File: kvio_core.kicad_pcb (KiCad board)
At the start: 6 copper layers, 60 x 41 mm, 214 parts, among them J1001 16-pin_FFC_(SFV16R), J1101 16-pin_FFC_(SFV16R), J1301 USB3_B_Micro, J301 Conn_01x06_Male, J401 16-pin_FFC_(SFV16R), J501 16-pin_FFC_(SFV16R), J601 16-pin_FFC_(SFV16R), J701 16-pin_FFC_(SFV16R), J801 16-pin_FFC_(SFV16R), J901 16-pin_FFC_(SFV16R), U1001 EMI8143, U101 xc7a100t-csg324, U1101 EMI8143, U1201 MT41J128M16JT-125:K, U1301 FT601Q, U1302 EMI8143, U201 FAN53541, U202 FAN53541, U203 FAN53541, U204 FAN53541, U301 MX25L3233F, U302 MAX809, U401 EMI8143, U501 EMI8143, U601 EMI8143, U701 EMI8143, U801 EMI8143, U901 EMI8143, Y1301 Crystal_GND24_Small

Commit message: More layout and design
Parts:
- removed R304, R305, R306, R309: 1k, passive:R_0402
- added R1001: 100, passive:R_0402, F.Cu at (128.7, 136.2)
- added R1002: 100, passive:R_0402, F.Cu at (128.7, 138.0)
- added R1003: 100, passive:R_0402, F.Cu at (131.3, 136.2)
- added R1101: 100, passive:R_0402, F.Cu at (138.5, 129.3)
- added R1102: 100, passive:R_0402, F.Cu at (138.5, 131.2)
- added R1103: 100, passive:R_0402, F.Cu at (141.1, 129.3)
- added R401: 100, passive:R_0402, F.Cu at (121.5, 122.5)
- added R402: 100, passive:R_0402, F.Cu at (118.8, 122.5)
- added R403: 100, passive:R_0402, F.Cu at (118.8, 124.3)
- added R501: 100, passive:R_0402, F.Cu at (118.8, 129.3)
- added R502: 100, passive:R_0402, F.Cu at (118.8, 131.2)
- added R503: 100, passive:R_0402, F.Cu at (121.5, 129.3)
- added R601: 100, passive:R_0402, F.Cu at (128.7, 122.5)
- added R602: 100, passive:R_0402, F.Cu at (128.7, 124.3)
- added R603: 100, passive:R_0402, F.Cu at (131.3, 122.5)
- added R701: 100, passive:R_0402, F.Cu at (118.8, 136.2)
- added R702: 100, passive:R_0402, F.Cu at (118.8, 138.0)
- added R703: 100, passive:R_0402, F.Cu at (121.5, 136.2)
- added R801: 100, passive:R_0402, F.Cu at (128.7, 129.3)
- added R802: 100, passive:R_0402, F.Cu at (131.3, 129.3)
- added R803: 100, passive:R_0402, F.Cu at (128.7, 131.2)
- added R901: 100, passive:R_0402, F.Cu at (138.5, 122.5)
- added R902: 100, passive:R_0402, F.Cu at (138.5, 124.3)
- added R903: 100, passive:R_0402, F.Cu at (141.1, 122.5)
- C216, C221, C227, C231, C233, C237, C241, C245, C249, C253, C254, C255, C261, C262, C263, C264, C265, C266, C267, C268, C269, C270, C285, C302, FB201, J1001, J1101, J401, J501, R310, U1001, U1101, U302, U401, U501: moved to B.Cu
- J301: footprint connectors:jst-sh-hor-6 -> Connector_PinSocket_1.27mm:PinSocket_2x03_P1.27mm_Vertical_SMD
- R1204: value 80 -> 100
- R301, R311, R312, R313, R314, R317, R318, R319, R320: value 33 -> 100
- R307, R315, R316: value 10k -> 4.7k
- moved C271 40.9 mm to (222.6, 75.8)
- moved C272 40.9 mm to (222.4, 76.6)
- moved C273 40.9 mm to (219.6, 78.3)
- moved C274 40.9 mm to (213.2, 75.9)
- moved C275 40.9 mm to (213.0, 76.6)
- moved C276 40.9 mm to (210.2, 78.3)
- moved C277 40.9 mm to (208.5, 75.9)
- moved C278 40.9 mm to (208.3, 76.6)
- moved C279 40.9 mm to (205.5, 78.3)
- moved C280 40.9 mm to (217.9, 75.9)
- moved C281 40.9 mm to (217.7, 76.6)
- moved C282 40.9 mm to (214.9, 78.3)
- moved L201 40.9 mm to (220.3, 75.8)
- moved L202 40.9 mm to (210.9, 75.8)
- moved L203 40.9 mm to (206.2, 75.8)
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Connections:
- C1305 pad 1: /USB3 Interface/3V3 -> +3V3
- C1306 pad 1: /USB3 Interface/3V3 -> +3V3
- C1308 pad 1: /USB3 Interface/3V3 -> +3V3
- C1309 pad 1: /USB3 Interface/3V3 -> +3V3
- C1313 pad 1: /USB3 Interface/3V3 -> +3V3
- C1314 pad 1: /USB3 Interface/3V3 -> +3V3
- C1316 pad 1: /USB3 Interface/3V3 -> +3V3
- C1317 pad 1: /USB3 Interface/3V3 -> +3V3
- C301 pad 2: /Config/3V3 -> +3V3
- C302 pad 2: /Config/3V3 -> +3V3
- R1302 pad 1: /USB3 Interface/3V3 -> +3V3
- R1303 pad 1: /USB3 Interface/3V3 -> +3V3
- R302 pad 2: /Config/3V3 -> +3V3
- R307 pad 1: /Config/3V3 -> +3V3
- R308 pad 1: /Config/3V3 -> +3V3
- R315 pad 1: /Config/3V3 -> +3V3
- R316 pad 1: /Config/3V3 -> +3V3
- U101 pad P11: /Config/CFG_MODE2 -> GND
- U101 pad P12: /Config/CFG_MODE0 -> +3V3
- U101 pad P13: /Config/CFG_MODE1 -> GND
- U101 pad P8: /Config/3V3 -> +3V3
- U101 pad P9: /Config/CFG_PROGRAM_B -> /Config/CFG_INIT_B
- U1301 pad 14: /USB3 Interface/3V3 -> +3V3
- U1301 pad 20: /USB3 Interface/3V3 -> +3V3
- U1301 pad 24: /USB3 Interface/3V3 -> +3V3
- U1301 pad 28: /USB3 Interface/3V3 -> +3V3
- U1301 pad 38: /USB3 Interface/3V3 -> +3V3
- U1301 pad 49: /USB3 Interface/3V3 -> +3V3
- U1301 pad 59: /USB3 Interface/3V3 -> +3V3
- U1301 pad 68: /USB3 Interface/3V3 -> +3V3
- U301 pad 8: /Config/3V3 -> +3V3
- U302 pad 3: /Config/3V3 -> +3V3
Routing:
- net GND: track 98.2 -> 147.8 mm, vias 83 -> 105
- net +3V3: track 7.87 -> 42.8 mm, vias 11 -> 33
- net +1V0: track 7.31 -> 31.9 mm, vias 10 -> 15
- net /USB3 Interface/3V3: track 19.4 -> 0.00 mm, vias 7 -> 0
- net +1V8: track 4.48 -> 15.9 mm, vias 5 -> 10
- net /DDR Memory/A4: track 21.5 -> 12.0 mm
- net /USB3 Interface/DATA_21: track 0.00 -> 8.69 mm, vias 0 -> 1
- net /USB3 Interface/DATA_7: track 0.00 -> 8.58 mm, vias 0 -> 1
- net /Config/CFG_INIT_B: track 0.00 -> 8.55 mm
- net /USB3 Interface/DATA_12: track 0.00 -> 8.34 mm, vias 0 -> 1
- net /USB3 Interface/DATA_1: track 0.00 -> 6.05 mm, vias 0 -> 1
- net /Config/CFG_DONE: track 0.00 -> 5.97 mm
- net /USB3 Interface/TXE_N: track 0.00 -> 5.93 mm, vias 0 -> 1
- net /USB3 Interface/DATA_10: track 0.00 -> 5.19 mm, vias 0 -> 1
- net /USB3 Interface/DATA_0: track 0.00 -> 5.16 mm, vias 0 -> 1
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- added copper zone on GND_PWR2, net +1V0
- added copper zone on GND_PWR2, net +1V8

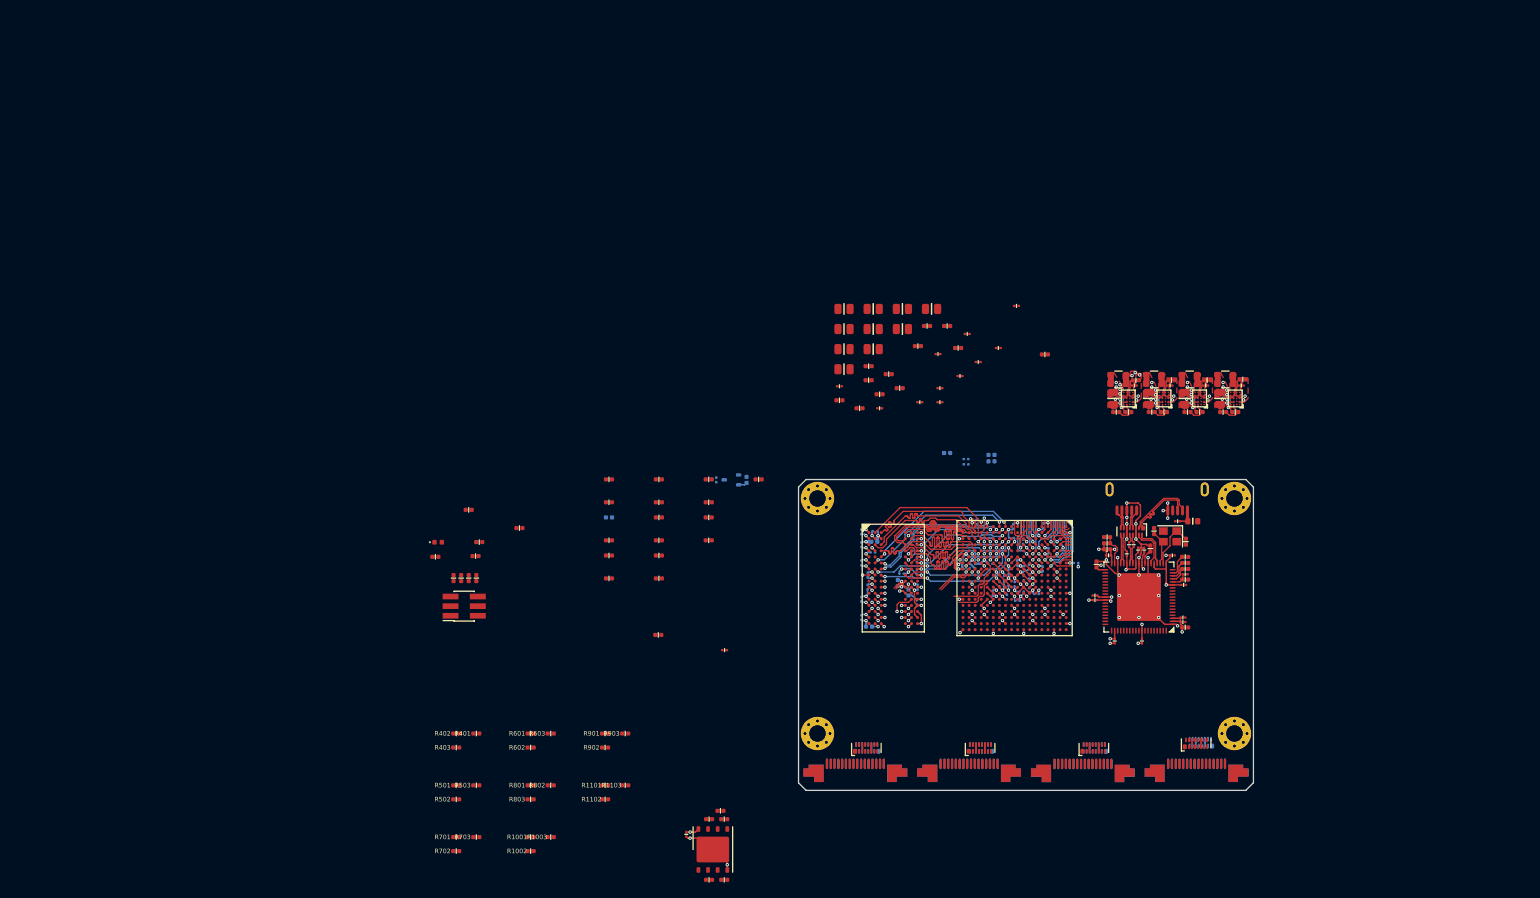
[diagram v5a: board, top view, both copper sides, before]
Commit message: Added 2 cameras via parallel interface
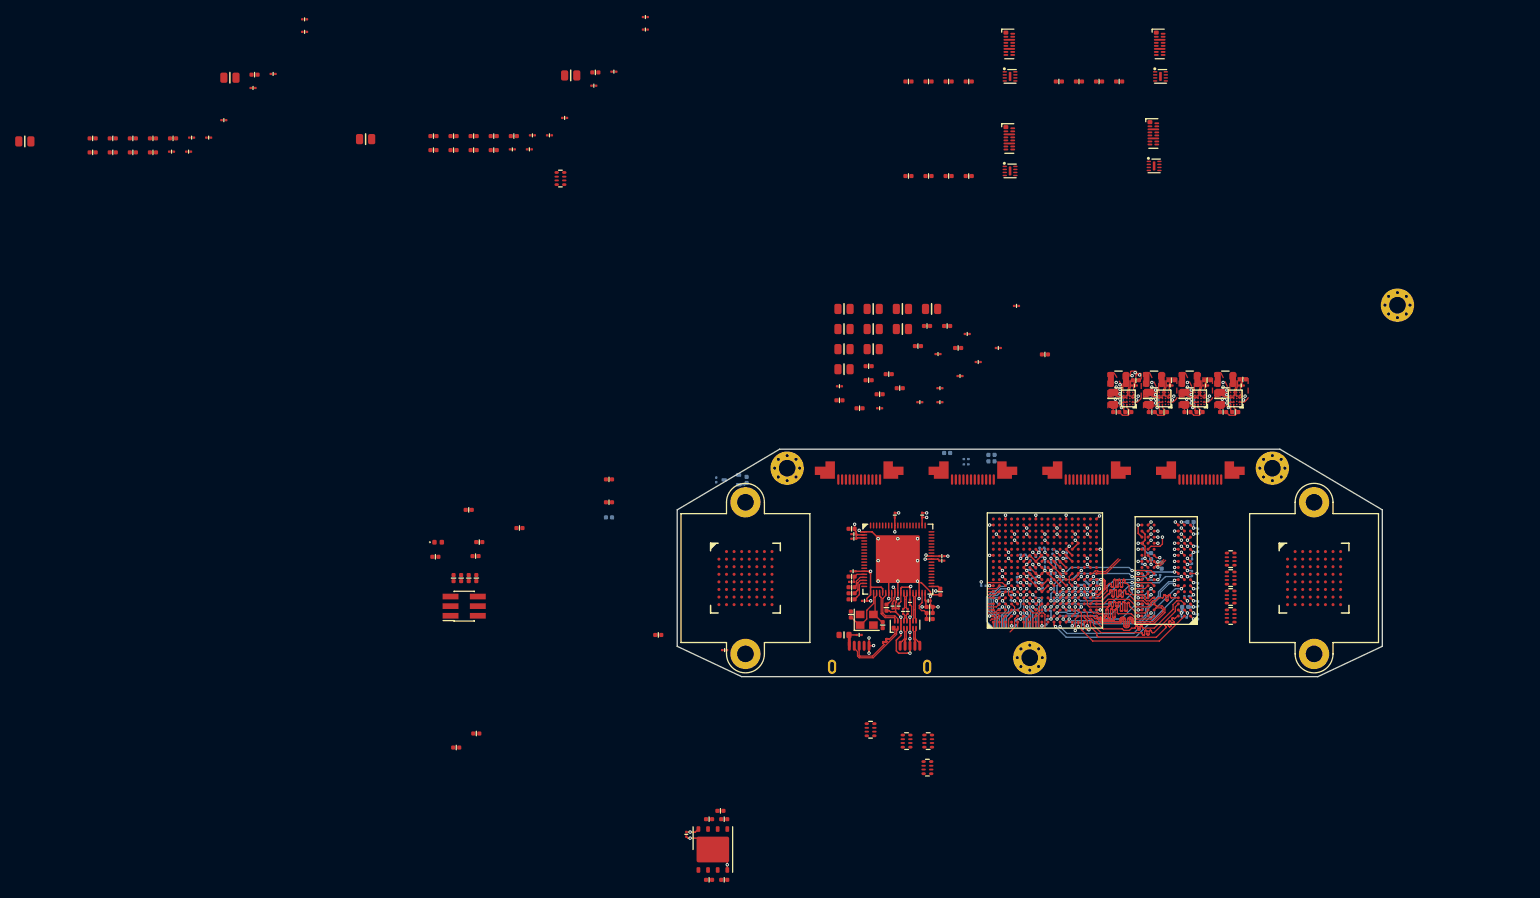
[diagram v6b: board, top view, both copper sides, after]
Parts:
- removed C501, C601, C701: 4.7u, passive:C_0402
- removed FB501, FB601, FB701: Ferrite_Bead_Small, passive:R_0402
- removed J1101, J501, J601, J701: 16-pin_FFC_(SFV16R), connectors:SFV16R
- removed R1003, R402, R501, R502, R503, R601, R602, R603, R701, R702, R703, R803, R903: 100, passive:R_0402
- removed U501, U601, U701: EMI8143, dfn:XDFN-16_1.35x3.5mm
- added C1102: 4.7u, passive:C_0402, F.Cu at (70.9, 44.0)
- added C1103: 4.7u, passive:C_0402, F.Cu at (92.2, 35.6)
- added C1104: 47u, passive:C_0805, F.Cu at (62.0, 44.4)
- added C1105: 0.1u, passive:C_0201, F.Cu at (94.7, 35.5)
- added C1106: 0.1u, passive:C_0201, F.Cu at (92.0, 37.4)
- added C1107: 4.7u, passive:C_0402, F.Cu at (73.5, 44.0)
- added C1108: 4.7u, passive:C_0402, F.Cu at (70.9, 45.9)
- added C1109: 4.7u, passive:C_0402, F.Cu at (73.5, 45.9)
- added C1110: 0.1u, passive:C_0201, F.Cu at (84.0, 43.9)
- added C1111: 0.1u, passive:C_0201, F.Cu at (98.8, 29.9)
- added C1112: 0.1u, passive:C_0201, F.Cu at (83.5, 45.8)
- added C1113: 0.1u, passive:C_0201, F.Cu at (88.2, 41.6)
- added C1114: 0.1u, passive:C_0201, F.Cu at (86.2, 43.9)
- added C1115: 0.1u, passive:C_0201, F.Cu at (98.8, 28.3)
- added C1116: 0.1u, passive:C_0201, F.Cu at (81.3, 45.8)
- added C1401: 47u, passive:C_0805, F.Cu at (106.9, 44.1)
- added C1402: 4.7u, passive:C_0402, F.Cu at (115.8, 43.7)
- added C1403: 4.7u, passive:C_0402, F.Cu at (118.5, 45.5)
- added C1404: 47u, passive:C_0805, F.Cu at (133.9, 35.7)
- added C1405: 0.1u, passive:C_0201, F.Cu at (143.8, 28.0)
- added C1406: 0.1u, passive:C_0201, F.Cu at (133.2, 41.3)
- added C1407: 4.7u, passive:C_0402, F.Cu at (115.8, 45.5)
- added C1408: 4.7u, passive:C_0402, F.Cu at (118.5, 43.7)
- added C1409: 4.7u, passive:C_0402, F.Cu at (137.2, 35.3)
- added C1410: 0.1u, passive:C_0201, F.Cu at (128.5, 45.5)
- added C1411: 0.1u, passive:C_0201, F.Cu at (143.8, 29.6)
- added C1412: 0.1u, passive:C_0201, F.Cu at (139.7, 35.2)
- added C1413: 0.1u, passive:C_0201, F.Cu at (128.9, 43.6)
- added C1414: 0.1u, passive:C_0201, F.Cu at (131.2, 43.6)
- added C1415: 0.1u, passive:C_0201, F.Cu at (137.0, 37.0)
- added C1416: 0.1u, passive:C_0201, F.Cu at (126.2, 45.5)
- added FB1401: Ferrite_Bead_Small, passive:R_0402, F.Cu at (123.8, 43.7)
- added LH1101: lens_holder, lensholders:m12_20mm, F.Cu at (157.0, 102.0)
- added LH1401: lens_holder, lensholders:m12_20mm, F.Cu at (232.0, 102.0)
- added R1104: 10k, passive:R_0402, F.Cu at (78.8, 45.9)
- added R1401: 10k, passive:R_0402, F.Cu at (121.2, 43.7)
- added R1402: 10k, passive:R_0402, F.Cu at (126.5, 43.7)
- added R1403: 10k, passive:R_0402, F.Cu at (121.2, 45.5)
- added R1404: 10k, passive:R_0402, F.Cu at (123.8, 45.5)
- added RN101: 22, passive:R_Array_Convex_4x0402, F.Cu at (132.6, 49.3)
- added RN1101: 22, passive:R_Array_Convex_4x0402, F.Cu at (221.0, 99.5)
- added RN1102: 22, passive:R_Array_Convex_4x0402, F.Cu at (221.0, 107.0)
- added RN1103: 22, passive:R_Array_Convex_4x0402, F.Cu at (221.0, 104.5)
- added RN1104: 22, passive:R_Array_Convex_4x0402, F.Cu at (221.0, 102.0)
- added RN1401: 22, passive:R_Array_Convex_4x0402, F.Cu at (181.0, 127.0)
- added RN1402: 22, passive:R_Array_Convex_4x0402, F.Cu at (181.1, 123.5)
- added RN1403: 22, passive:R_Array_Convex_4x0402, F.Cu at (173.5, 122.0)
- added RN1404: 22, passive:R_Array_Convex_4x0402, F.Cu at (178.2, 123.5)
- added U1002: EMI8143, dfn:XDFN-16_1.35x3.5mm, F.Cu at (211.6, 31.6)
- added U1401: AR0135CS, cameras:AR0135CS, F.Cu at (157.0, 102.0)
- added U402: IP4254CZ8-4-TTL, dfn:UDFN-8-1EP_1.7x1.35mm_P0.4mm_EP0.4x1.2mm, F.Cu at (210.9, 47.6)
- added U802: EMI8143, dfn:XDFN-16_1.35x3.5mm, F.Cu at (191.8, 31.6)
- added U902: EMI8143, dfn:XDFN-16_1.35x3.5mm, F.Cu at (191.8, 44.1)
- C1101: value 4.7u -> 47u; footprint passive:C_0402 -> passive:C_0805
- J1001, J401: value 16-pin_FFC_(SFV16R) -> 12-pin_FFC_(SFV12R); footprint connectors:SFV16R -> connectors:SFV12R; moved to F.Cu
- J801, J901: value 16-pin_FFC_(SFV16R) -> 12-pin_FFC_(SFV12R); footprint connectors:SFV16R -> connectors:SFV12R
- R1101, R1102, R1103: value 100 -> 10k
- U1001: value EMI8143 -> IP4254CZ8-4-TTL; footprint dfn:XDFN-16_1.35x3.5mm -> dfn:UDFN-8-1EP_1.7x1.35mm_P0.4mm_EP0.4x1.2mm; moved to F.Cu
- U1101: value EMI8143 -> AR0135CS; footprint dfn:XDFN-16_1.35x3.5mm -> cameras:AR0135CS; moved to F.Cu
- U401: moved to F.Cu
- U801, U901: value EMI8143 -> IP4254CZ8-4-TTL; footprint dfn:XDFN-16_1.35x3.5mm -> dfn:UDFN-8-1EP_1.7x1.35mm_P0.4mm_EP0.4x1.2mm
- moved R1002 124.6 mm to (201.0, 36.5)
- moved R1001 121.6 mm to (198.3, 36.5)
- moved R801 108.0 mm to (183.8, 36.5)
- moved R802 108.0 mm to (186.4, 36.5)
- moved R1103 105.8 mm to (76.2, 45.9)
- moved R1102 104.2 mm to (81.5, 44.0)
- moved R1101 104.1 mm to (78.8, 44.0)
- moved FB1101 94.0 mm to (76.2, 44.0)
- moved U401 89.4 mm to (210.8, 43.4), turned to 0 degrees
- moved C1001 89.3 mm to (206.3, 36.5)
- moved U801 89.3 mm to (191.9, 35.8), turned to 0 degrees
- moved U1001 89.0 mm to (211.7, 35.8), turned to 0 degrees
- moved C1101 87.8 mm to (89.0, 36.0)
- moved R902 86.6 mm to (181.2, 49.0)
- moved R901 86.4 mm to (183.8, 49.0)
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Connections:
- C1101 pad 1: Net-(C1101-Pad1) -> +1V8
- FB1001 pad 2: /Camera 7/5V -> /Camera 4/5V
- FB1101 pad 1: Net-(C1101-Pad1) -> /sheet5D568411/VPLL
- FB1101 pad 2: /Camera 8/5V -> VAA
- FB801 pad 2: /Camera 5/5V -> /Camera 2/5V
- FB901 pad 2: /Camera 6/5V -> /Camera 3/5V
- J1001 pad 10: GND -> Net-(J1001-Pad10)
- J1001 pad 11: /Camera 7/IO1 -> Net-(J1001-Pad11)
- J1001 pad 12: /Camera 7/IO2 -> Net-(C1001-Pad1)
- J401 pad 10: GND -> Net-(J401-Pad10)
- J401 pad 11: /Camera 1/IO1 -> Net-(J401-Pad11)
- J401 pad 12: /Camera 1/IO2 -> Net-(C401-Pad1)
- J801 pad 10: GND -> Net-(J801-Pad10)
- J801 pad 11: /Camera 5/IO1 -> Net-(J801-Pad11)
- J801 pad 12: /Camera 5/IO2 -> Net-(C801-Pad1)
- J901 pad 10: GND -> Net-(J901-Pad10)
- J901 pad 11: /Camera 6/IO1 -> Net-(J901-Pad11)
- J901 pad 12: /Camera 6/IO2 -> Net-(C901-Pad1)
- R1001 pad 1: /Camera 7/D1_P -> /Camera 4/D1_P
- R1001 pad 2: /Camera 7/D1_N -> /Camera 4/D1_N
- R1002 pad 1: /Camera 7/D2_P -> /Camera 4/CLK_P
- R1002 pad 2: /Camera 7/D2_N -> /Camera 4/CLK_N
- R1101 pad 1: /Camera 8/D1_P -> /CAM_RESET
- R1101 pad 2: /Camera 8/D1_N -> GND
- R1102 pad 1: /Camera 8/D2_P -> Net-(R1102-Pad1)
- R1102 pad 2: /Camera 8/D2_N -> GND
- R1103 pad 1: /Camera 8/CLK_P -> /sheet5D568411/SADDR
- R1103 pad 2: /Camera 8/CLK_N -> GND
- R801 pad 1: /Camera 5/D1_P -> /Camera 2/D1_P
- R801 pad 2: /Camera 5/D1_N -> /Camera 2/D1_N
- R802 pad 1: /Camera 5/D2_P -> /Camera 2/CLK_P
- R802 pad 2: /Camera 5/D2_N -> /Camera 2/CLK_N
- R901 pad 1: /Camera 6/D1_P -> /Camera 3/D1_P
- R901 pad 2: /Camera 6/D1_N -> /Camera 3/D1_N
- R902 pad 1: /Camera 6/D2_P -> /Camera 3/CLK_P
- R902 pad 2: /Camera 6/D2_N -> /Camera 3/CLK_N
- U1001 pad 1: Net-(J1001-Pad9) -> /Camera 4/IO1
- U1001 pad 2: Net-(J1001-Pad8) -> /Camera 4/IO2
- U1001 pad 3: GND -> /Camera 4/SDA
- U1001 pad 4: Net-(J1001-Pad6) -> /Camera 4/SCL
- U1001 pad 5: Net-(J1001-Pad5) -> Net-(J1001-Pad11)
- U1001 pad 6: GND -> Net-(J1001-Pad10)
- U1001 pad 7: Net-(J1001-Pad3) -> Net-(J1001-Pad9)
- U1001 pad 8: Net-(J1001-Pad2) -> Net-(J1001-Pad8)
- U1001 pad 9: /Camera 7/D1_N -> GND
- U101 pad L18: Net-(U101-PadL18) -> /CAM0_D1
- U101 pad M13: Net-(U101-PadM13) -> /CAM0_D5
- U101 pad M16: Net-(U101-PadM16) -> /CAM0_FV
- U101 pad M17: Net-(U101-PadM17) -> /CAM0_LV
- U101 pad M18: Net-(U101-PadM18) -> /CAM0_D2
- U101 pad N14: Net-(U101-PadN14) -> /CAM0_D8
- U101 pad N15: Net-(U101-PadN15) -> /CAM0_TRIGGER
- U101 pad N16: Net-(U101-PadN16) -> /CAM0_FLASH
- U101 pad N17: Net-(U101-PadN17) -> /CAM0_D10
- U101 pad P14: Net-(U101-PadP14) -> /CAM0_D9
- U101 pad P15: Net-(U101-PadP15) -> /CAM0_PIXCLK
- U101 pad P17: Net-(U101-PadP17) -> /CAM0_SDATA
- U101 pad P18: Net-(U101-PadP18) -> /CAM0_D11
- U101 pad R10: Net-(U101-PadR10) -> /CAM_RESET
- U101 pad R11: Net-(U101-PadR11) -> /CAM0_D0
- U101 pad R12: Net-(U101-PadR12) -> /CAM0_D3
- U101 pad R13: Net-(U101-PadR13) -> /CAM0_D4
- U101 pad R15: Net-(U101-PadR15) -> /CAM1_PIXCLK
- U101 pad R17: Net-(U101-PadR17) -> /CAM0_SCLK
- U101 pad R18: Net-(U101-PadR18) -> /CAM0_D6
- U101 pad T10: Net-(U101-PadT10) -> /CAM_CLK
- U101 pad T11: Net-(U101-PadT11) -> /CAM1_D7
- U101 pad T13: Net-(U101-PadT13) -> /CAM1_FLASH
- U101 pad T14: Net-(U101-PadT14) -> /CAM1_D0
- U101 pad T15: Net-(U101-PadT15) -> /CAM1_D1
- U101 pad T18: Net-(U101-PadT18) -> /CAM0_D7
- U101 pad T9: Net-(U101-PadT9) -> /CAM1_SCLK
- U101 pad U11: Net-(U101-PadU11) -> /CAM1_D8
- U101 pad U12: Net-(U101-PadU12) -> /CAM1_D9
- U101 pad U13: Net-(U101-PadU13) -> /CAM1_SDATA
- U101 pad U14: Net-(U101-PadU14) -> /CAM1_LV
- U101 pad U16: Net-(U101-PadU16) -> /CAM1_D5
- U101 pad U17: Net-(U101-PadU17) -> /CAM1_D3
- U101 pad U18: Net-(U101-PadU18) -> /CAM1_D4
- U101 pad V10: Net-(U101-PadV10) -> /CAM1_D11
- U101 pad V11: Net-(U101-PadV11) -> /CAM1_FV
- U101 pad V12: Net-(U101-PadV12) -> /CAM1_D10
- U101 pad V14: Net-(U101-PadV14) -> /CAM1_TRIGGER
- U101 pad V16: Net-(U101-PadV16) -> /CAM1_D2
- U101 pad V17: Net-(U101-PadV17) -> /CAM1_D6
- U401 pad 1: Net-(J401-Pad9) -> Net-(U401-Pad1)
- U401 pad 12: /Camera 1/D2_N -> /Camera 1/CLK_N
- U401 pad 13: /Camera 1/D2_P -> /Camera 1/CLK_P
- U401 pad 15: /Camera 1/CLK_N -> GND
- U401 pad 16: /Camera 1/CLK_P -> GND
- U401 pad 2: Net-(J401-Pad8) -> Net-(U401-Pad2)
- U801 pad 1: Net-(J801-Pad9) -> /Camera 2/IO1
- U801 pad 2: Net-(J801-Pad8) -> /Camera 2/IO2
- U801 pad 3: GND -> /Camera 2/SDA
- U801 pad 4: Net-(J801-Pad6) -> /Camera 2/SCL
- U801 pad 5: Net-(J801-Pad5) -> Net-(J801-Pad11)
- U801 pad 6: GND -> Net-(J801-Pad10)
- U801 pad 7: Net-(J801-Pad3) -> Net-(J801-Pad9)
- U801 pad 8: Net-(J801-Pad2) -> Net-(J801-Pad8)
- U801 pad 9: /Camera 5/D1_N -> GND
- U901 pad 1: Net-(J901-Pad9) -> /Camera 3/IO1
- U901 pad 2: Net-(J901-Pad8) -> /Camera 3/IO2
- U901 pad 3: GND -> /Camera 3/SDA
- U901 pad 4: Net-(J901-Pad6) -> /Camera 3/SCL
- U901 pad 5: Net-(J901-Pad5) -> Net-(J901-Pad11)
- U901 pad 6: GND -> Net-(J901-Pad10)
- U901 pad 7: Net-(J901-Pad3) -> Net-(J901-Pad9)
- U901 pad 8: Net-(J901-Pad2) -> Net-(J901-Pad8)
- U901 pad 9: /Camera 6/D1_N -> GND
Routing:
- net /Config/CFG_INIT_B: track 8.55 -> 1.93 mm
- net /Config/CFG_DONE: track 5.97 -> 0.00 mm
- net /DDR Memory/BA1: track 18.6 -> 14.0 mm
- net /DDR Memory/A9: track 25.7 -> 22.0 mm
- net /DDR Memory/WE_N: track 27.9 -> 25.3 mm
- net /USB3 Interface/DATA_26: track 1.67 -> 2.51 mm
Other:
- board size 60 x 41 mm -> 93 x 30 mm
